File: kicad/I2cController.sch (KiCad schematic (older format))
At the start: 23 parts, among them J1 CONN_02X03, J2 CONN_01X06, J3 CONN_02X02, Q1 Q_NPN_CBE, SW1 Start, SW2 Stop, SW3 WeldCurv, SW4 Rotary_Encoder_Switch_V2, U1 MCP23017

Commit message: Kicad project  mistake correction
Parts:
- Q1: symbol Q_NPN_CBE -> Q_NPN_EBC
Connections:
- net Gnd_P: now also Q1.1 (E); no longer Q1.3 (E)
- net at DS1.16 (LED-): now also Q1.3 (C); no longer Q1.1 (C)
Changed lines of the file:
@@
 LIBS:atmel
 LIBS:audio
+LIBS:Battery_Management
 LIBS:bbd
+LIBS:Bosch
 LIBS:brooktre
 LIBS:cmos4000
 LIBS:conn
+LIBS:Connector
 LIBS:contrib
 LIBS:cypress
 LIBS:dc-dc
+LIBS:Decawave
 LIBS:device
 LIBS:digital-audio
+LIBS:Diode
+LIBS:Display
+LIBS:driver_gate
 LIBS:dsp
+LIBS:DSP_Microchip_DSPIC33
 LIBS:elec-unifil
 LIBS:ESD_Protection
+LIBS:Espressif
+LIBS:FPGA_Actel
 LIBS:ftdi
 LIBS:gennum
+LIBS:Graphic
 LIBS:hc11
+LIBS:infineon
 LIBS:intel
 LIBS:interface
+LIBS:intersil
 LIBS:ir
 LIBS:Lattice
+LIBS:LED
+LIBS:LEM
 LIBS:linear
+LIBS:Logic_74xgxx
+LIBS:Logic_74xx
+LIBS:Logic_CMOS_4000
+LIBS:Logic_CMOS_IEEE
+LIBS:logic_programmable
+LIBS:Logic_TTL_IEEE
 LIBS:maxim
+LIBS:MCU_Microchip_PIC10
+LIBS:MCU_Microchip_PIC12
+LIBS:MCU_Microchip_PIC16
+LIBS:MCU_Microchip_PIC18
+LIBS:MCU_Microchip_PIC24
+LIBS:MCU_Microchip_PIC32
+LIBS:MCU_NXP_Kinetis
+LIBS:MCU_NXP_LPC
+LIBS:MCU_NXP_S08
+LIBS:MCU_Parallax
+LIBS:MCU_ST_STM8
+LIBS:MCU_ST_STM32
+LIBS:MCU_Texas_MSP430
+LIBS:Mechanical
 LIBS:memory
 LIBS:microchip
 LIBS:microcontrollers
+LIBS:modules
+LIBS:Motor
 LIBS:motor_drivers
 LIBS:motorola
+LIBS:Msystem
 LIBS:nordicsemi
+LIBS:nxp
 LIBS:onsemi
 LIBS:opto
@@
 LIBS:references
 LIBS:regul
+LIBS:Relay
 LIBS:relays
+LIBS:RF_Bluetooth
 LIBS:rfcom
+LIBS:RFSolutions
+LIBS:Sensor_Current
+LIBS:Sensor_Humidity
 LIBS:sensors
 LIBS:silabs
 LIBS:siliconi
 LIBS:supertex
+LIBS:Switch
 LIBS:switches
 LIBS:texas
+LIBS:Transformer
+LIBS:Transistor
 LIBS:transistors
+LIBS:triac_thyristor
+LIBS:Valve
 LIBS:valves
 LIBS:video
@@
 LIBS:zetex
 LIBS:Zilog
+LIBS:arduino
 LIBS:HotAirGun-cache
 EELAYER 25 0
@@
 $EndComp
 $Comp
-L Q_NPN_CBE Q1
+L Q_NPN_EBC Q1
 U 1 1 5C09B046
 P 2950 2950

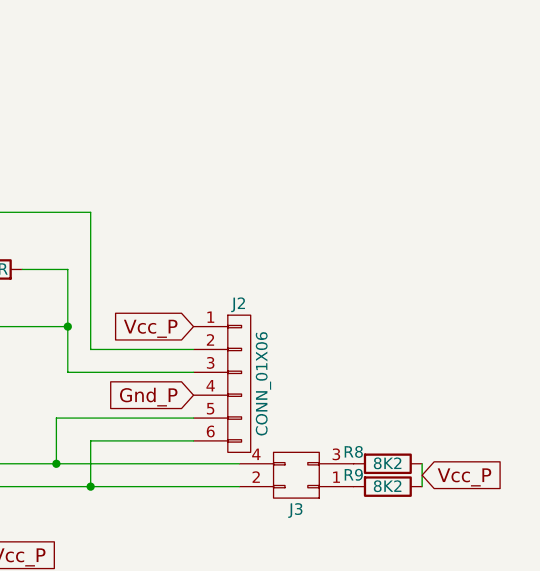
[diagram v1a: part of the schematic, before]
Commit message: Added C5 bypass capacitor
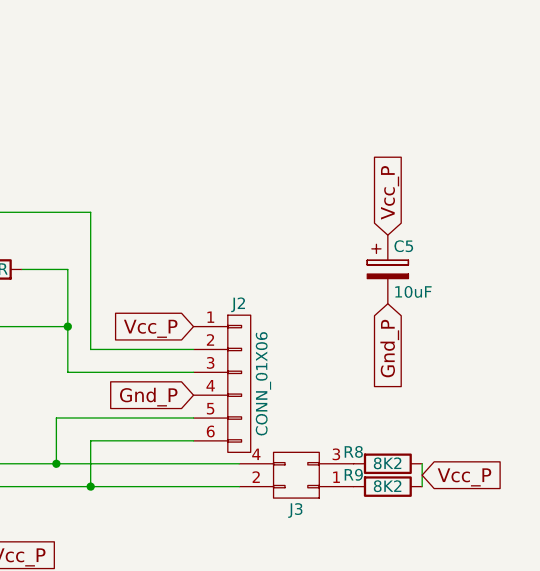
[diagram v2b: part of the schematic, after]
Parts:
- added C5: 10uF, Capacitors_THT:CP_Radial_D10.0mm_P5.00mm, symbol CP
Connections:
- net Gnd_P: now also C5.2
- net Vcc_P: now also C5.1
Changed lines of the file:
@@
 	7100 3750 7100 3250
 Connection ~ 7100 3250
+$Comp
+L CP C5
+U 1 1 5CE7B713
+P 9400 2100
+F 0 "C5" H 9425 2200 50  0000 L CNN
+F 1 "10uF" H 9425 2000 50  0000 L CNN
+F 2 "Capacitors_THT:CP_Radial_D10.0mm_P5.00mm" H 9438 1950 50  0001 C CNN
+F 3 "" H 9400 2100 50  0001 C CNN
+	1    9400 2100
+	1    0    0    -1
+$EndComp
+Text GLabel 9400 1950 1    60   Input ~ 0
+Vcc_P
+Text GLabel 9400 2250 3    60   Input ~ 0
+Gnd_P
 $EndSCHEMATC

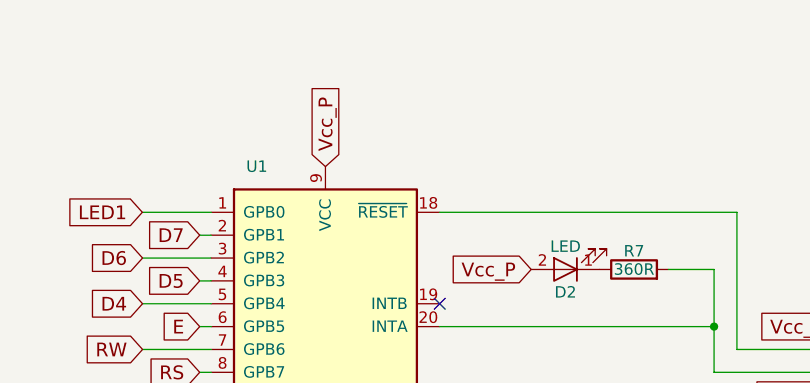
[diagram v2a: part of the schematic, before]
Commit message: Added C6 bypass capacitor
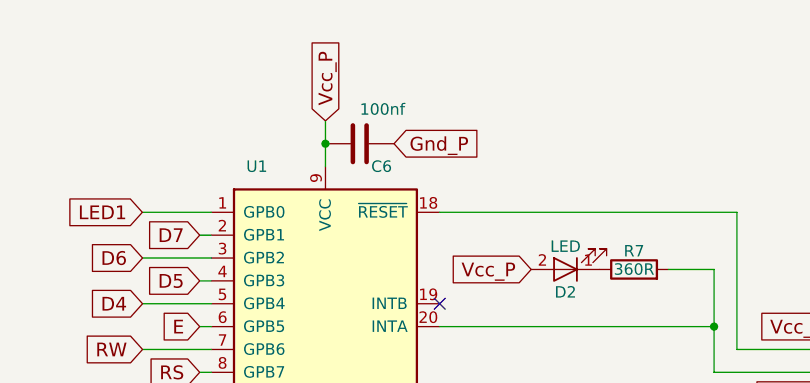
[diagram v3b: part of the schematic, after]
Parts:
- added C6: 100nf, Capacitors_SMD:C_0603_HandSoldering, symbol C
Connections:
- net Gnd_P: now also C6.1
- net Vcc_P: now also C6.2
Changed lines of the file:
@@
 Wire Wire Line
 	1750 1850 1750 2600
-Text GLabel 6300 1650 1    60   Input ~ 0
+Text GLabel 6300 1450 1    60   Input ~ 0
 Vcc_P
 Text GLabel 7600 3350 2    60   Input ~ 0
@@
 Text GLabel 9400 2250 3    60   Input ~ 0
 Gnd_P
+$Comp
+L C C6
+U 1 1 5CE7F5AB
+P 6450 1550
+F 0 "C6" V 6550 1600 50  0000 L CNN
+F 1 "100nf" V 6300 1550 50  0000 L CNN
+F 2 "Capacitors_SMD:C_0603_HandSoldering" H 6488 1400 50  0001 C CNN
+F 3 "" H 6450 1550 50  0001 C CNN
+	1    6450 1550
+	0    1    1    0
+$EndComp
+Wire Wire Line
+	6300 1450 6300 1650
+Connection ~ 6300 1550
+Text GLabel 6600 1550 2    60   Input ~ 0
+Gnd_P
 $EndSCHEMATC
